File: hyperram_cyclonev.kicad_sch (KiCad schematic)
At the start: 69 parts, among them IC1 AP63205WU, IC2 TXB0108PWR, IC3 S26KL128SDABHI020, IC4 W25Q32JVSSIQ_TR, IC5 S27KL0641DABHI020, J1 ASP-122952-01, J2 HDMI_A, J3 1156915, J4 1156915, J5 Conn_02x06_Top_Bottom, J6 Conn_02x06_Top_Bottom, J7 Conn_02x06_Top_Bottom, J8 1156915, J9 1156915, Q1 BSS138, Q2 BSS138

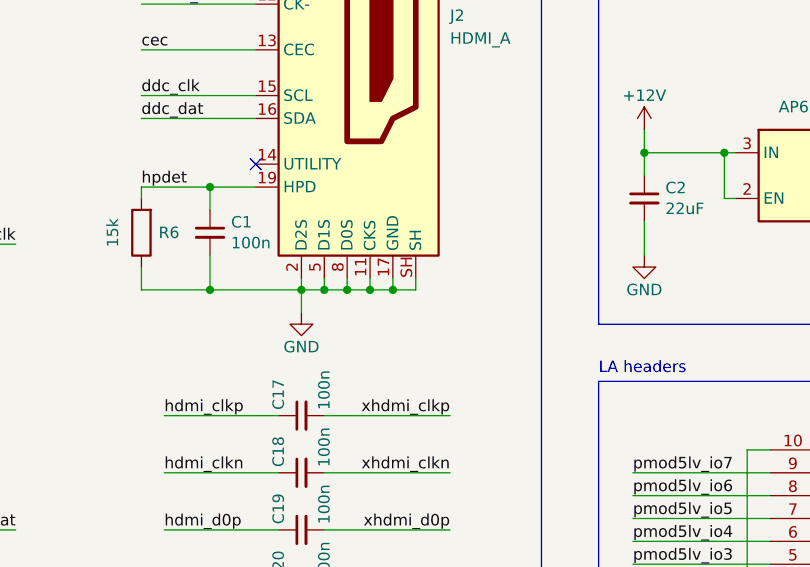
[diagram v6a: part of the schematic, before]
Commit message: Loaded components into PCB.
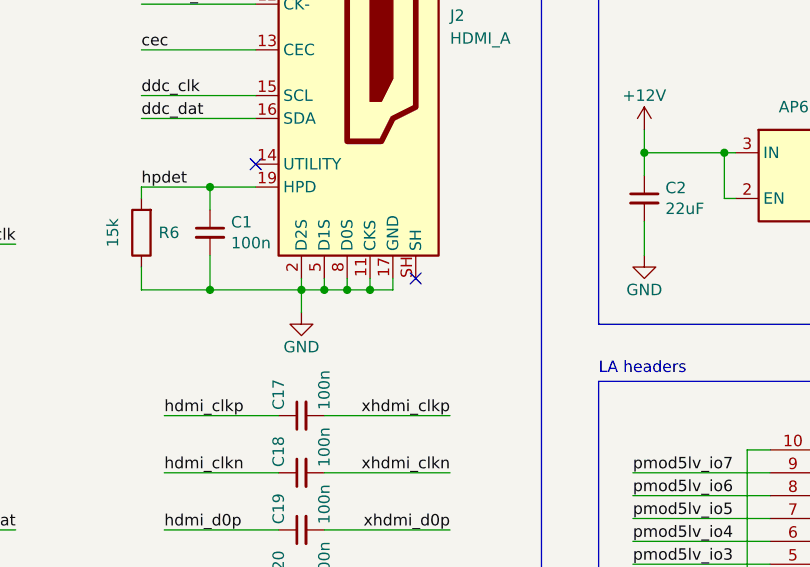
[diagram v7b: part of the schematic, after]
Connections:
- net GND: no longer J2.SH
- no-connect marks 7 -> 8
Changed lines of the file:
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@@
 	)
 	(junction
-		(at 104.14 85.09)
-		(diameter 0)
-		(color 0 0 0 0)
-	)
-	(junction
 		(at 140.97 69.85)
 		(diameter 0)
@@
 	)
 	(no_connect
+		(at 106.68 83.82)
+	)
+	(no_connect
 		(at 350.52 120.65)
 	)
@@
 	(wire
 		(pts
-			(xy 106.68 85.09) (xy 104.14 85.09)
-		)
-		(stroke
-			(width 0)
-			(type default)
-		)
-	)
-	(wire
-		(pts
 			(xy 125.73 226.06) (xy 139.7 226.06)
 		)
@@
 		)
 		(stroke
-			(width 0)
-			(type default)
-		)
-	)
-	(wire
-		(pts
-			(xy 106.68 83.82) (xy 106.68 85.09)
-		)
-		(stroke

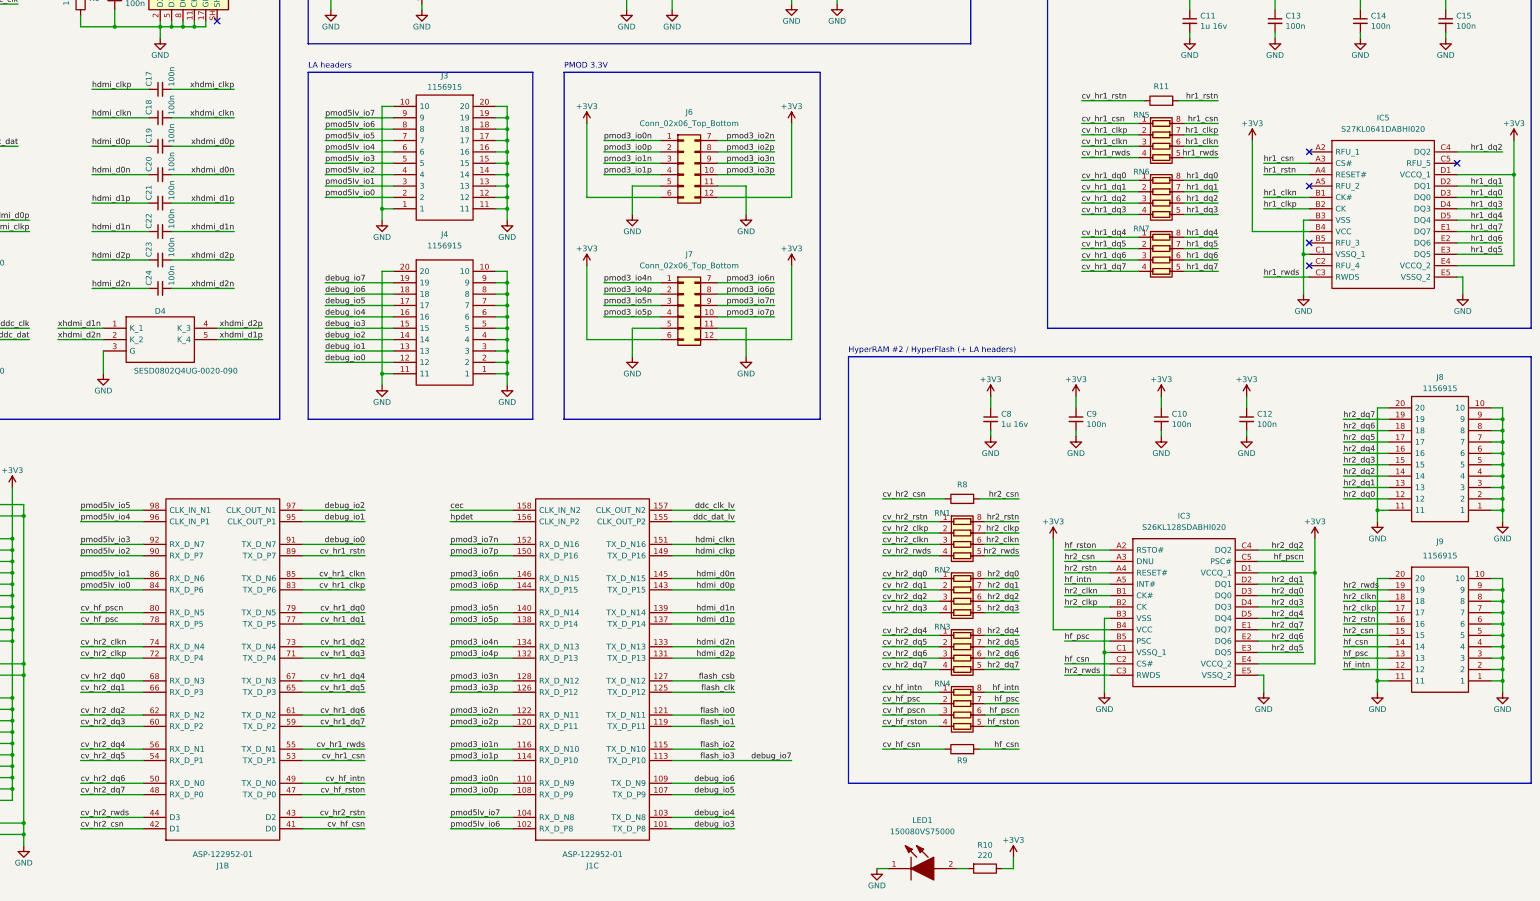
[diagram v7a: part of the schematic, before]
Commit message: Simplified schematic, removing unnecessary elements
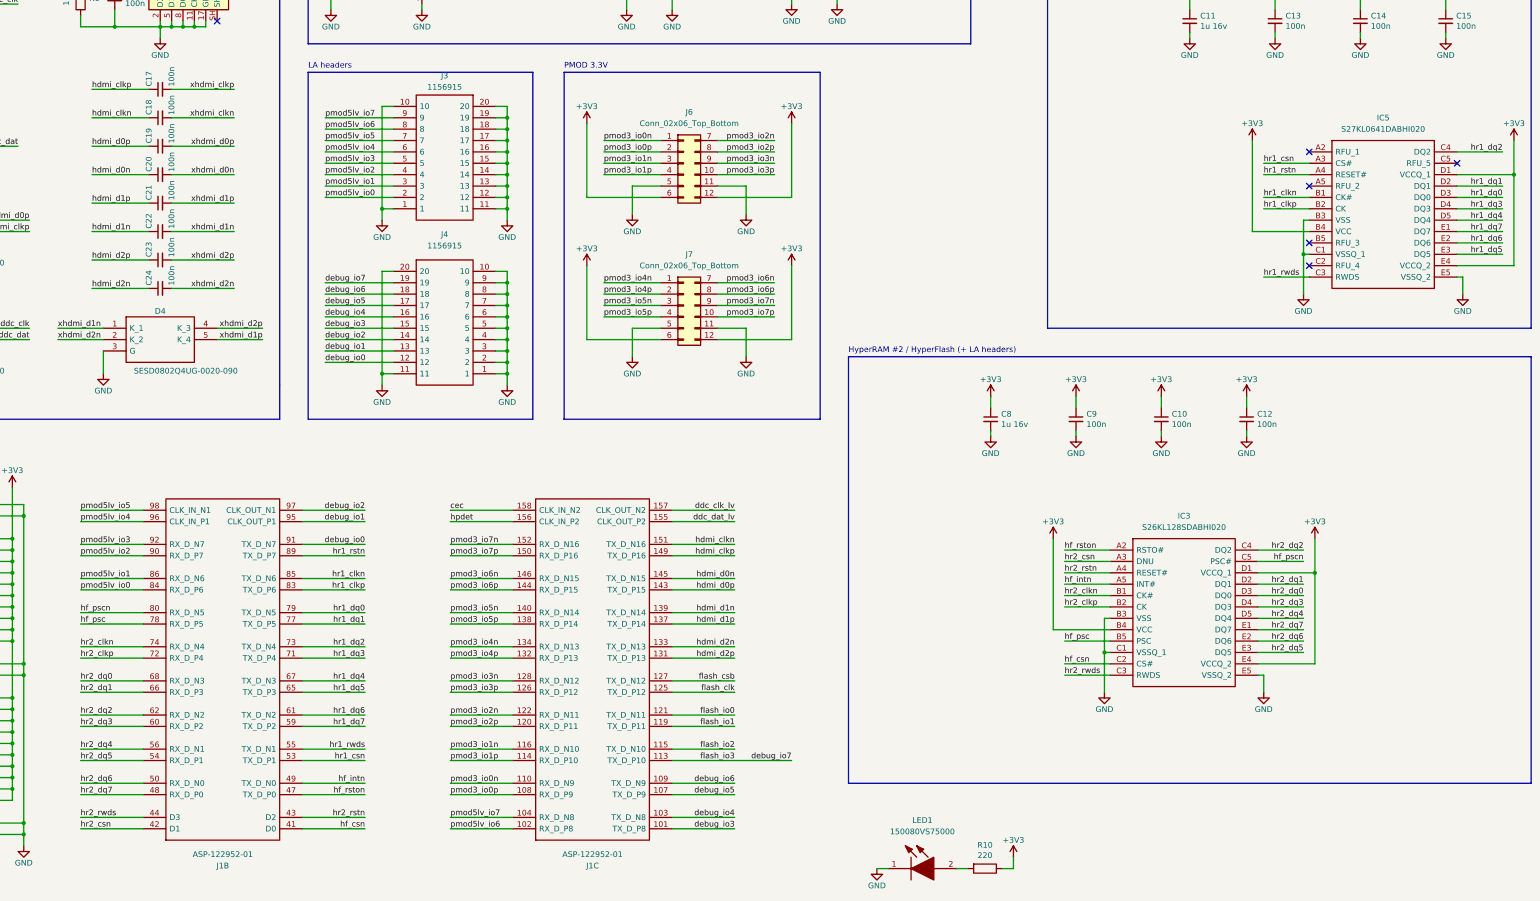
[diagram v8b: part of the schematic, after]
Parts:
- removed J8, J9: 1156915, hyperram_cyclonev:1156915, symbol hyperram_cyclonev:1156915
- removed R11, R8, R9: R, Resistor_SMD:R_0603_1608Metric_Pad0.98x0.95mm_HandSolder, symbol Device:R
- removed RN1, RN2, RN3, RN4, RN5, RN6, RN7: CAY16-22R0F4LF, hyperram_cyclonev:CAY16000J4LF, symbol Device:R_Pack04
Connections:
- net cv_hf_csn is gone; now on net hf_csn: J1.41 (D0)
- net cv_hf_intn is gone; now on net hf_intn: J1.49 (TX_D_N0)
- net cv_hf_psc is gone; now on net hf_psc: J1.78 (RX_D_P5)
- net cv_hf_pscn is gone; now on net hf_pscn: J1.80 (RX_D_N5)
- net cv_hf_rston is gone; now on net hf_rston: J1.47 (TX_D_P0)
- net cv_hr1_clkn is gone; now on net hr1_clkn: J1.85 (TX_D_N6)
- net cv_hr1_clkp is gone; now on net hr1_clkp: J1.83 (TX_D_P6)
- net cv_hr1_csn is gone; now on net hr1_csn: J1.53 (TX_D_P1)
- net cv_hr1_dq0 is gone; now on net hr1_dq0: J1.79 (TX_D_N5)
- net cv_hr1_dq1 is gone; now on net hr1_dq1: J1.77 (TX_D_P5)
- net cv_hr1_dq2 is gone; now on net hr1_dq2: J1.73 (TX_D_N4)
- net cv_hr1_dq3 is gone; now on net hr1_dq3: J1.71 (TX_D_P4)
- net cv_hr1_dq4 is gone; now on net hr1_dq4: J1.67 (TX_D_N3)
- net cv_hr1_dq5 is gone; now on net hr1_dq5: J1.65 (TX_D_P3)
- net cv_hr1_dq6 is gone; now on net hr1_dq6: J1.61 (TX_D_N2)
- net cv_hr1_dq7 is gone; now on net hr1_dq7: J1.59 (TX_D_P2)
- net cv_hr1_rstn is gone; now on net hr1_rstn: J1.89 (TX_D_P7)
- net cv_hr1_rwds is gone; now on net hr1_rwds: J1.55 (TX_D_N1)
- net cv_hr2_clkn is gone; now on net hr2_clkn: J1.74 (RX_D_N4)
- net cv_hr2_clkp is gone; now on net hr2_clkp: J1.72 (RX_D_P4)
- net cv_hr2_csn is gone; now on net hr2_csn: J1.42 (D1)
- net cv_hr2_dq0 is gone; now on net hr2_dq0: J1.68 (RX_D_N3)
- net cv_hr2_dq1 is gone; now on net hr2_dq1: J1.66 (RX_D_P3)
- net cv_hr2_dq2 is gone; now on net hr2_dq2: J1.62 (RX_D_N2)
- net cv_hr2_dq3 is gone; now on net hr2_dq3: J1.60 (RX_D_P2)
- net cv_hr2_dq4 is gone; now on net hr2_dq4: J1.56 (RX_D_N1)
- net cv_hr2_dq5 is gone; now on net hr2_dq5: J1.54 (RX_D_P1)
- net cv_hr2_dq6 is gone; now on net hr2_dq6: J1.50 (RX_D_N0)
- net cv_hr2_dq7 is gone; now on net hr2_dq7: J1.48 (RX_D_P0)
- net cv_hr2_rstn is gone; now on net hr2_rstn: J1.43 (D2)
- net cv_hr2_rwds is gone; now on net hr2_rwds: J1.44 (D3)
